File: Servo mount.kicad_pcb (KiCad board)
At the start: 2 copper layers, 80 x 34.1 mm, 40 parts, among them IC1 ATTINY84-SS, J1 SOLDER_PAD, J2 SOLDER_PAD, J3 SOLDER_PAD, J5 +5V, J6 GND, J7 SOLDER_PAD, J8 SOLDER_PAD, K5 CONN_3, K6 CONN_3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

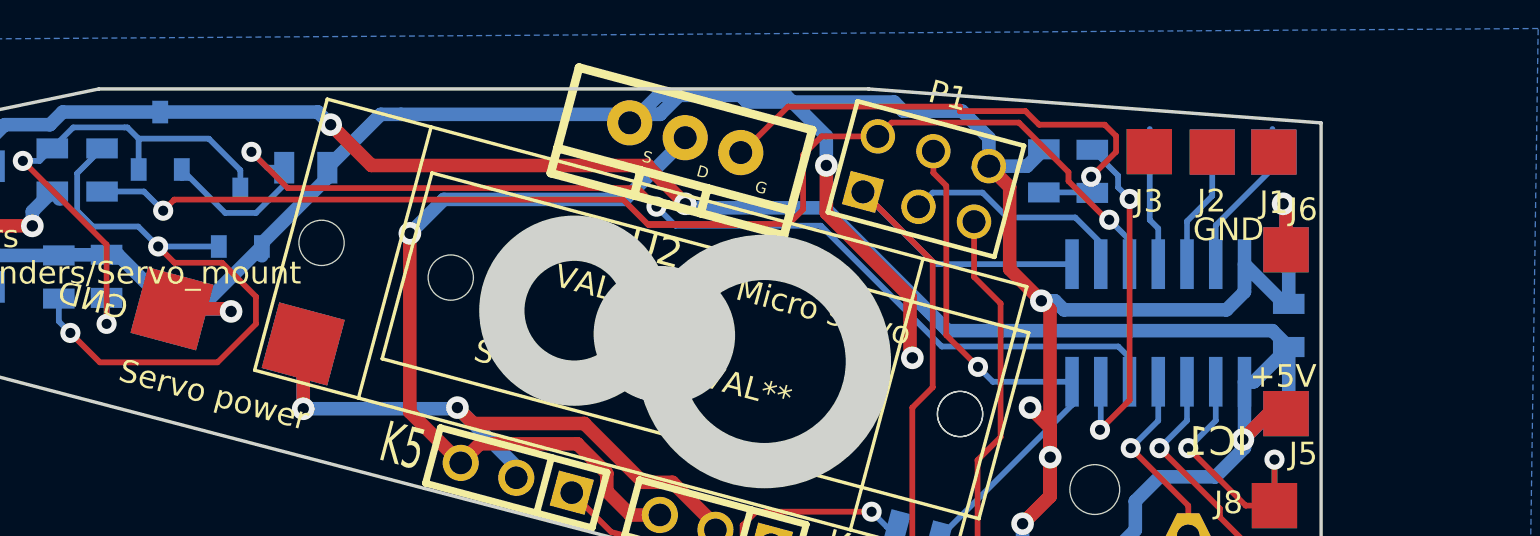
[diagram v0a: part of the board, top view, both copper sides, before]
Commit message: fix footprints Q1 and Q2
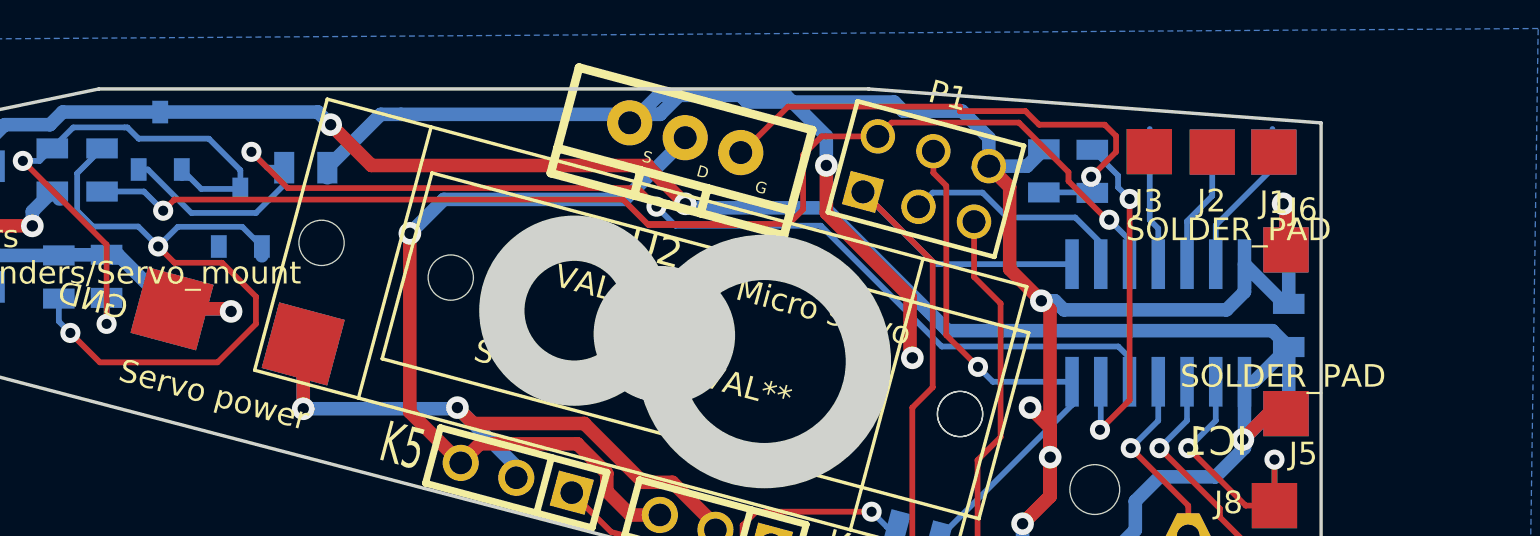
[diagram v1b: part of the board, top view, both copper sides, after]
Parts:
- J5: value +5V -> SOLDER_PAD
- J6: value GND -> SOLDER_PAD
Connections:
- Q1 pad 1: GND -> Net-(Q1-Pad1)
- Q1 pad 2: Net-(Q1-Pad2) -> GND
- Q2 pad 1: Rail signal -> Net-(C8-Pad1)
- Q2 pad 2: Net-(C8-Pad1) -> Rail signal
- R7 pad 2: Net-(Q1-Pad2) -> Net-(Q1-Pad1)
- R8 pad 2: Net-(Q1-Pad2) -> Net-(Q1-Pad1)
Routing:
- net Net-(Q1-Pad1): track 0.00 -> 30.9 mm, vias 0 -> 2
- net Net-(Q1-Pad2): track 27.7 -> 0.00 mm, vias 2 -> 0
- net GND: track 155.4 -> 146.8 mm
- net Net-(C8-Pad1): track 23.1 -> 25.0 mm
- net Rail signal: track 53.5 -> 55.0 mm

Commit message: Updates to rev. 3x
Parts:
- removed Micro servo: VAL**, Micro_servo
- SG90_: footprint Pyth_servos:Micro_servo_SG90 -> Pyth_servos:Combined_servo
- moved SG90_ 2.94 mm to (152.8, 111.3), turned to 345 degrees
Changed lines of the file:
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@@
     (tracks 380)
     (zones 0)
-    (modules 40)
+    (modules 39)
     (nets 26)
   )
@@
       (net 2 -VAA))
   )
-  (module Micro_servo (layer F.Cu)
-    (at 152.8 111.35 345)
-    (tags HD-1370A)
-    (fp_text reference "Micro servo" (at 4.65 -2.8 345) (layer F.SilkS)
-      (effects (font (size 1 1) (thickness 0.15)))
-    )
-    (fp_text value VAL** (at 2.25 1.3 345) (layer F.SilkS)
-      (effects (font (size 1 1) (thickness 0.15)))
-    )
-    (fp_circle (center -2 0) (end 0 -0.2) (layer Edge.Cuts) (width 2))
-    (fp_circle (center -6 0) (end -3.5 2) (layer Edge.Cuts) (width 2))
-    (fp_line (start 13.65 4.25) (end -13.65 4.25) (layer F.SilkS) (width 0.15))
-    (fp_line (start -13.65 -4.25) (end 13.65 -4.25) (layer F.SilkS) (width 0.15))
-    (fp_line (start 13.65 -4.25) (end 13.65 4.25) (layer F.SilkS) (width 0.15))
-    (fp_line (start -13.65 -4.25) (end -13.65 4.25) (layer F.SilkS) (width 0.15))
-    (pad "" np_thru_hole circle (at -11.65 0 345) (size 2 2) (drill 2) (layers *.Cu *.Mask F.SilkS))
-    (pad "" np_thru_hole circle (at 11.65 0 345) (size 2 2) (drill 2) (layers *.Cu *.Mask F.SilkS))
-  )
   (module solder_jumper_conn (layer F.Cu)
     (at 174.13 120.95 90)
@@
     (pad 1 smd rect (at -0.9525 -1.27 180) (size 0.70104 1.00076) (layers B.Cu B.Paste B.Mask)
       (net 25 "Net-(Q1-Pad1)"))
-    (model smd/SOT23_6.wrl
+    (model smd/smd_transistors/sot23.wrl
       (at (xyz 0 0 0))
-      (scale (xyz 0.11 0.11 0.11))
-      (rotate (xyz 0 0 -180))
+      (scale (xyz 1 1 1))
+      (rotate (xyz 0 0 0))
     )
   )
@@
     (model smd/smd_transistors/sot23.wrl
       (at (xyz 0 0 0))
-      (scale (xyz 0.11 0.11 0.11))
-      (rotate (xyz 0 0 -180))
+      (scale (xyz 1 1 1))
+      (rotate (xyz 0 0 0))
     )
   )
@@
       (net 3 AGND))
   )
-  (module Pyth_servos:Micro_servo_SG90 (layer F.Cu)
-    (at 149.94 110.58 165)
-    (tags SG90)
-    (fp_text reference SG90_ (at 4.65 -2.8 165) (layer F.SilkS)
-      (effects (font (size 1 1) (thickness 0.15)))
-    )
-    (fp_text value VAL** (at 2.25 1.3 165) (layer F.SilkS)
-      (effects (font (size 1 1) (thickness 0.15)))
-    )
-    (fp_line (start 11.25 -6.2) (end 11.25 6.2) (layer F.SilkS) (width 0.15))
-    (fp_line (start -11.25 -6.2) (end -11.25 6.2) (layer F.SilkS) (width 0.15))
-    (fp_circle (center -1.2 0) (end 0.8 -0.2) (layer Edge.Cuts) (width 2))
-    (fp_circle (center -5.65 0) (end -1.05 0) (layer Edge.Cuts) (width 2))
-    (fp_line (start 16 6.2) (end -16 6.2) (layer F.SilkS) (width 0.15))
-    (fp_line (start -16 -6.2) (end 16 -6.2) (layer F.SilkS) (width 0.15))
-    (fp_line (start 16 -6.2) (end 16 6.2) (layer F.SilkS) (width 0.15))
-    (fp_line (start -16 -6.2) (end -16 6.2) (layer F.SilkS) (width 0.15))
-    (pad "" np_thru_hole circle (at -14.6 0 165) (size 2 2) (drill 2) (layers *.Cu *.Mask F.SilkS))
-    (pad "" np_thru_hole circle (at 14.6 0 165) (size 2 2) (drill 2) (layers *.Cu *.Mask F.SilkS))
-    (model ../Pyth_kicad_lib/models/Servo_SG90.wrl
-      (at (xyz 0 0 0))
-      (scale (xyz 1 1 1))
-      (rotate (xyz 0 0 0))
-    )
-  )
   (module Pyth:solder_pad_2mm_fb (layer F.Cu)
     (at 178.448 114.346)
@@
       (effects (font (size 1 1) (thickness 0.15)))
     )
-    (fp_text value SOLDER_PAD (at -0.127 -1.651) (layer F.SilkS)
+    (fp_text value SOLDER_PAD (at -0.127 -1.651) (layer F.SilkS) hide
       (effects (font (size 1 1) (thickness 0.15)))
     )
@@
       (effects (font (size 1 1) (thickness 0.15)))
     )
-    (fp_text value SOLDER_PAD (at -2.54 -0.889) (layer F.SilkS)
+    (fp_text value SOLDER_PAD (at -2.54 -0.889) (layer F.SilkS) hide
       (effects (font (size 1 1) (thickness 0.15)))
     )
@@
       (net 14 "Net-(IC1-Pad2)"))
   )
+  (module Pyth_servos:Combined_servo (layer F.Cu)
+    (at 152.794 111.298 345)
+    (tags HD-1370A)
+    (fp_text reference SG90_ (at 4.65 -2.8 345) (layer F.SilkS)
+      (effects (font (size 1 1) (thickness 0.15)))
+    )
+    (fp_text value VAL** (at 2.25 1.3 345) (layer F.SilkS)
+      (effects (font (size 1 1) (thickness 0.15)))
+    )
+    (fp_circle (center 0 0) (end 12.55 7) (layer F.SilkS) (width 0.15))
+    (fp_line (start 13.65 4.25) (end -13.65 4.25) (layer F.SilkS) (width 0.15))
+    (fp_line (start -13.65 -4.25) (end 13.65 -4.25) (layer F.SilkS) (width 0.15))
+    (fp_line (start 13.65 -4.25) (end 13.65 4.25) (layer F.SilkS) (width 0.15))
+    (fp_line (start -13.65 -4.25) (end -13.65 4.25) (layer F.SilkS) (width 0.15))
+    (fp_circle (center -6 0) (end -1.75 0) (layer Edge.Cuts) (width 0.1))
+    (fp_line (start -14.2 -6.205) (end -14.2 6.195) (layer F.SilkS) (width 0.15))
+    (fp_line (start 8.3 -6.205) (end 8.3 6.195) (layer F.SilkS) (width 0.15))
+    (fp_circle (center -1.75 0) (end -3.75 -0.005) (layer Edge.Cuts) (width 0.1))
+    (fp_circle (center 2.7 0) (end -1.9 -0.005) (layer Edge.Cuts) (width 0.1))
+    (fp_line (start -18.95 6.2) (end 13.05 6.2) (layer F.SilkS) (width 0.15))
+    (fp_line (start 13.05 -6.2) (end -18.95 -6.2) (layer F.SilkS) (width 0.15))
+    (fp_line (start -18.95 -6.2) (end -18.95 6.2) (layer F.SilkS) (width 0.15))
+    (fp_line (start 13.05 -6.2) (end 13.05 6.2) (layer F.SilkS) (width 0.15))
+    (pad "" np_thru_hole circle (at -11.65 0 345) (size 2 2) (drill 2) (layers *.Cu *.Mask F.SilkS))
+    (pad "" np_thru_hole circle (at 11.65 0 345) (size 2 2) (drill 2) (layers *.Cu *.Mask F.SilkS))
+    (pad "" np_thru_hole circle (at -17.55 0 165) (size 2 2) (drill 2) (layers *.Cu *.Mask F.SilkS))
+    (model ../Pyth_kicad_lib/models/Servo_SG90.wrl
+      (at (xyz 0 0 0))
+      (scale (xyz 1 1 1))
+      (rotate (xyz 0 0 0))
+    )
+  )
   (gr_line (start 106 134.08) (end 108.94 134.08) (angle 90) (layer Edge.Cuts) (width 0.15))
